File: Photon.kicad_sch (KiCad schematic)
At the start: 39 parts, among them P1 USB_C_Plug_USB2.0, SW1 TS-1088-AR02016, SW2 TS-1088-AR02016, U1 ATtiny13A-S, U2 RT8059GJ5, U3 BCR421UW6-7, U4 BCR421UW6-7, U5 TP4056, U6 FS8205A, U7 DW01A

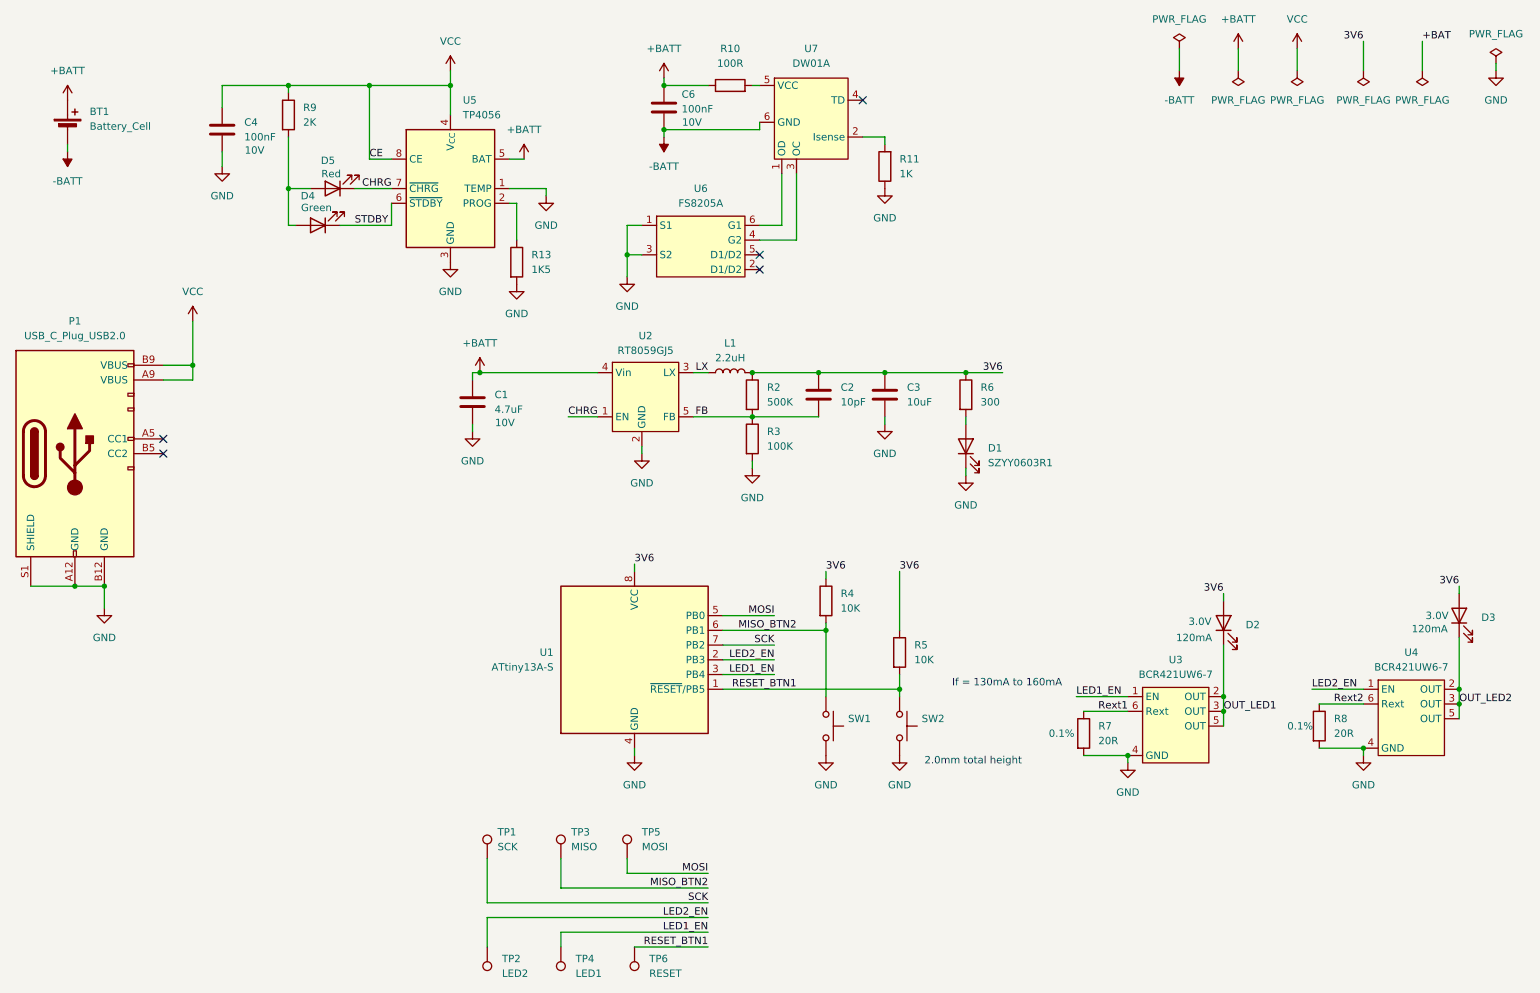
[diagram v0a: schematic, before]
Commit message: made new pcb. and updated schematic
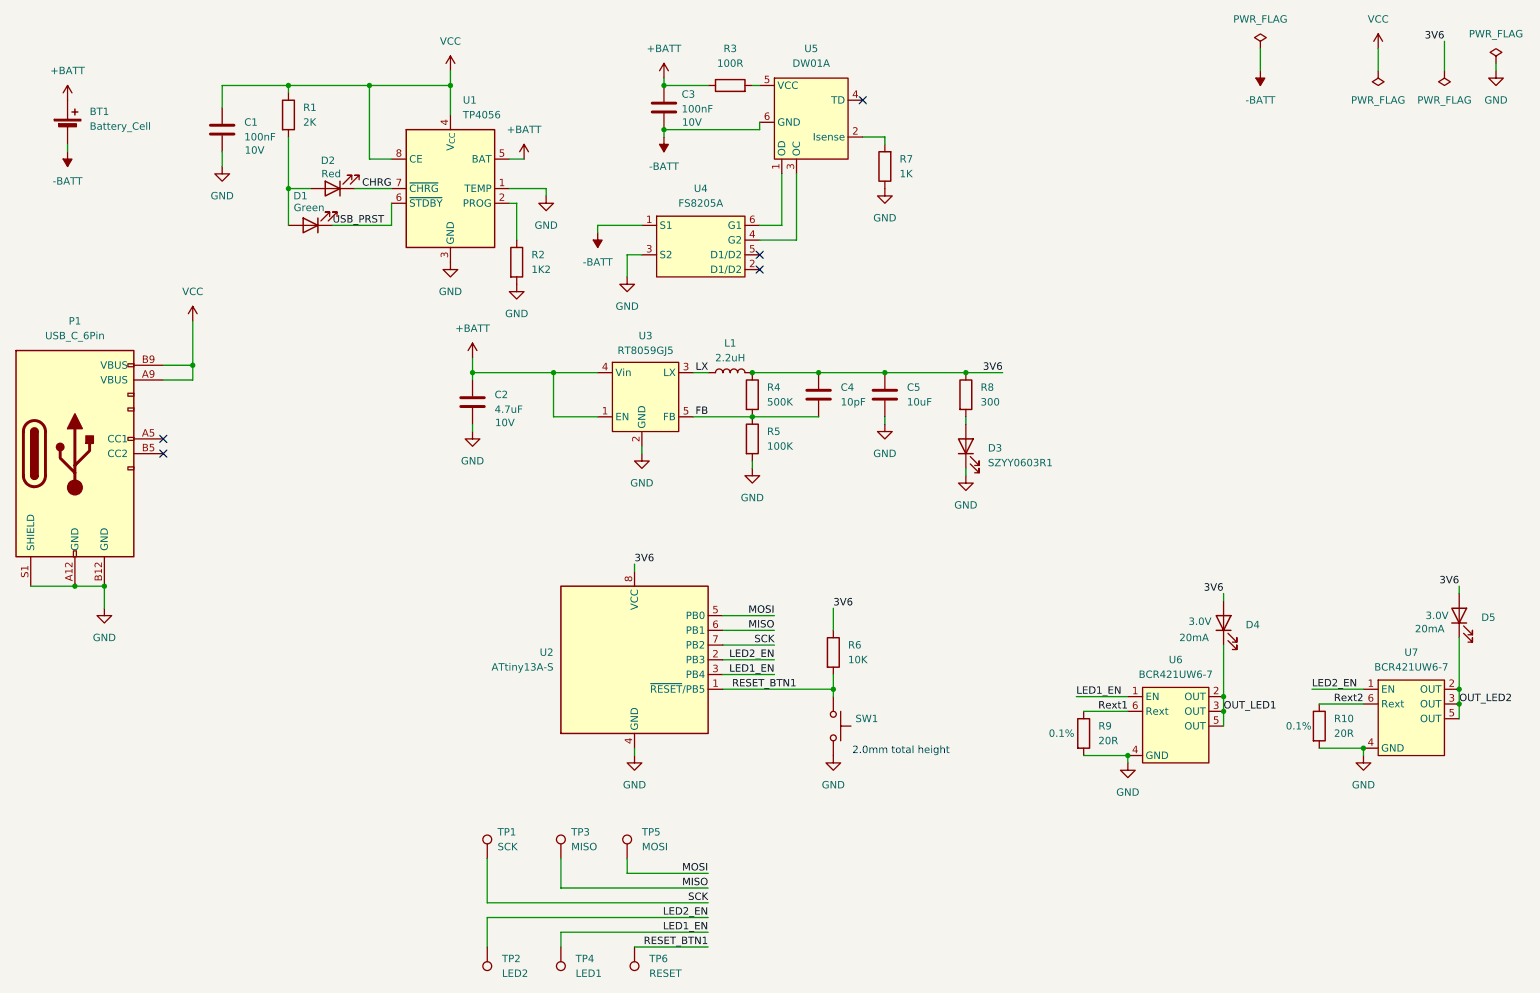
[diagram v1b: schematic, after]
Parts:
- removed R4: 10K, Resistor_SMD:R_0603_1608Metric, symbol Device:R
- removed SW1: TS-1088-AR02016, Photon:5mm Push Button, symbol Switch:SW_Push
- D4: renamed from D2; If 120mA -> 20mA
- D5: renamed from D3; If 120mA -> 20mA
- P1: value USB_C_Plug_USB2.0 -> USB_C_6Pin; footprint Photon:USB_C_Through_Hole -> Connector_USB:USB_C_Receptacle_GCT_USB4125-xx-x-0190_6P_TopMnt_Horizontal
- R2: renamed from R13; value 1K5 -> 1K2
- renumbered C4 to C1, C1 to C2, C6 to C3, C2 to C4, C3 to C5, D4 to D1, D5 to D2, D1 to D3, R9 to R1, R8 to R10, R10 to R3, R2 to R4, R3 to R5, R5 to R6, R11 to R7, R6 to R8, R7 to R9, SW2 to SW1, U5 to U1, U1 to U2, U2 to U3, U6 to U4, U7 to U5, U3 to U6, U4 to U7
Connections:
- net +BATT: now also U3.1 (EN)
- net -BATT: now also U4.1 (S1)
- net CHRG: no longer U3.1 (EN)
- net GND: no longer U4.1 (S1)
- net MISO_BTN2 renamed MISO
- net STDBY renamed USB_PRST
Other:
- note removed: "If = 130mA to 160mA"
- moved on the sheet: D1, R6, SW1

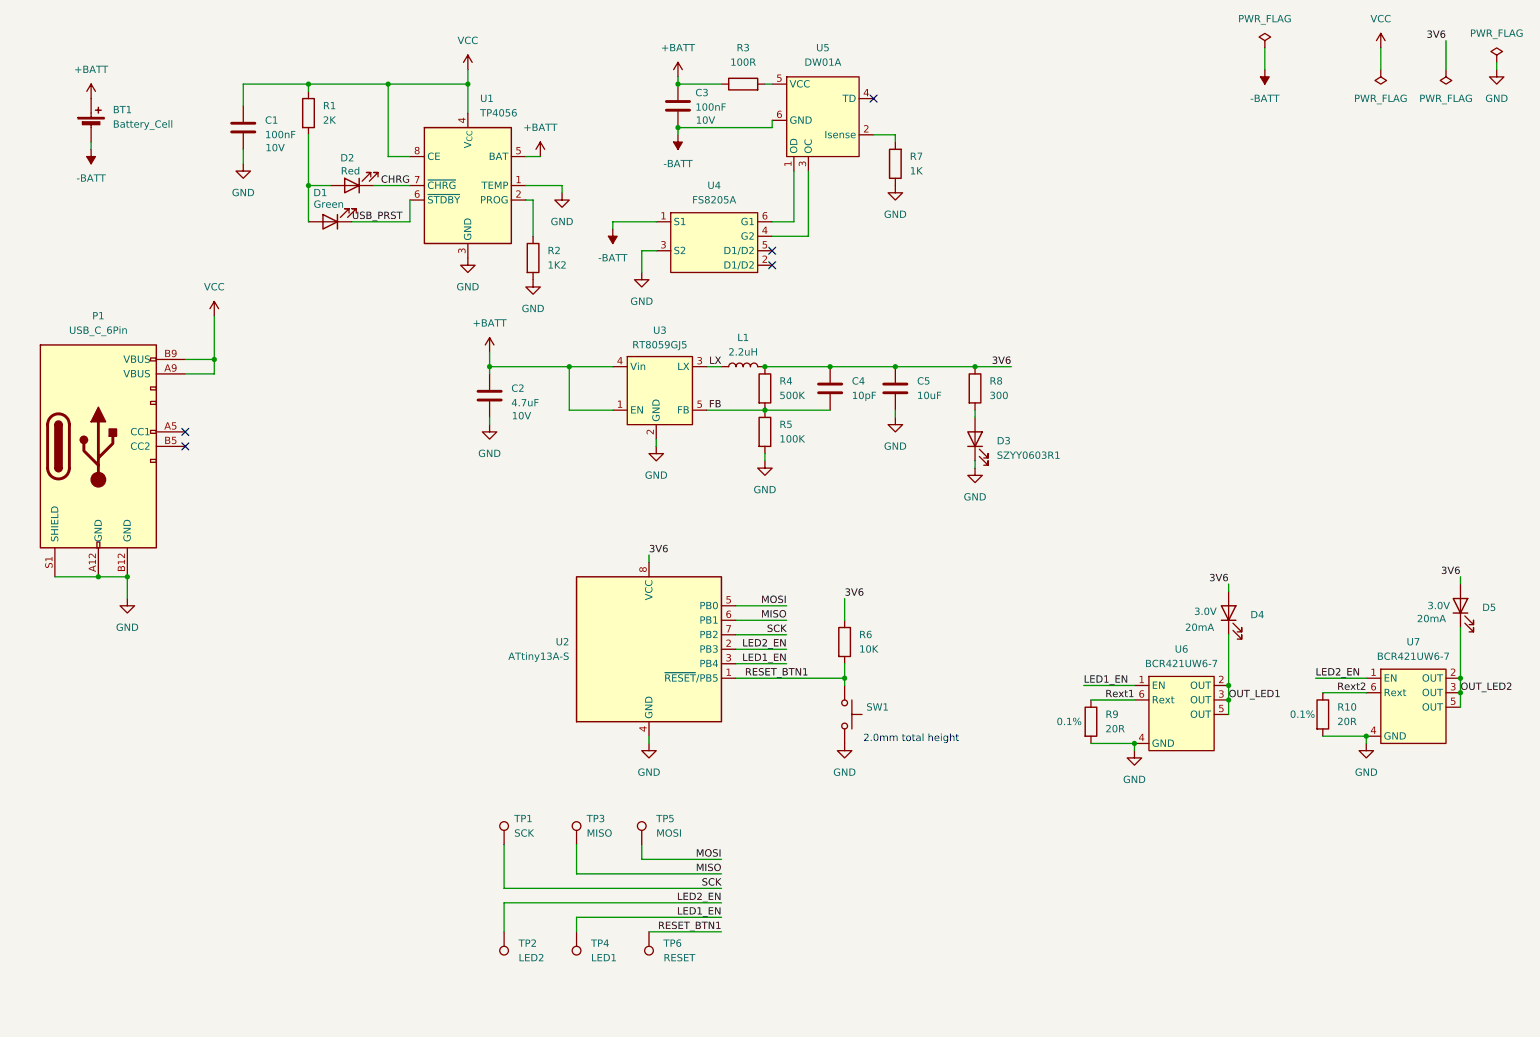
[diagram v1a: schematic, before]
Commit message: Cleaned up schematic and PCB
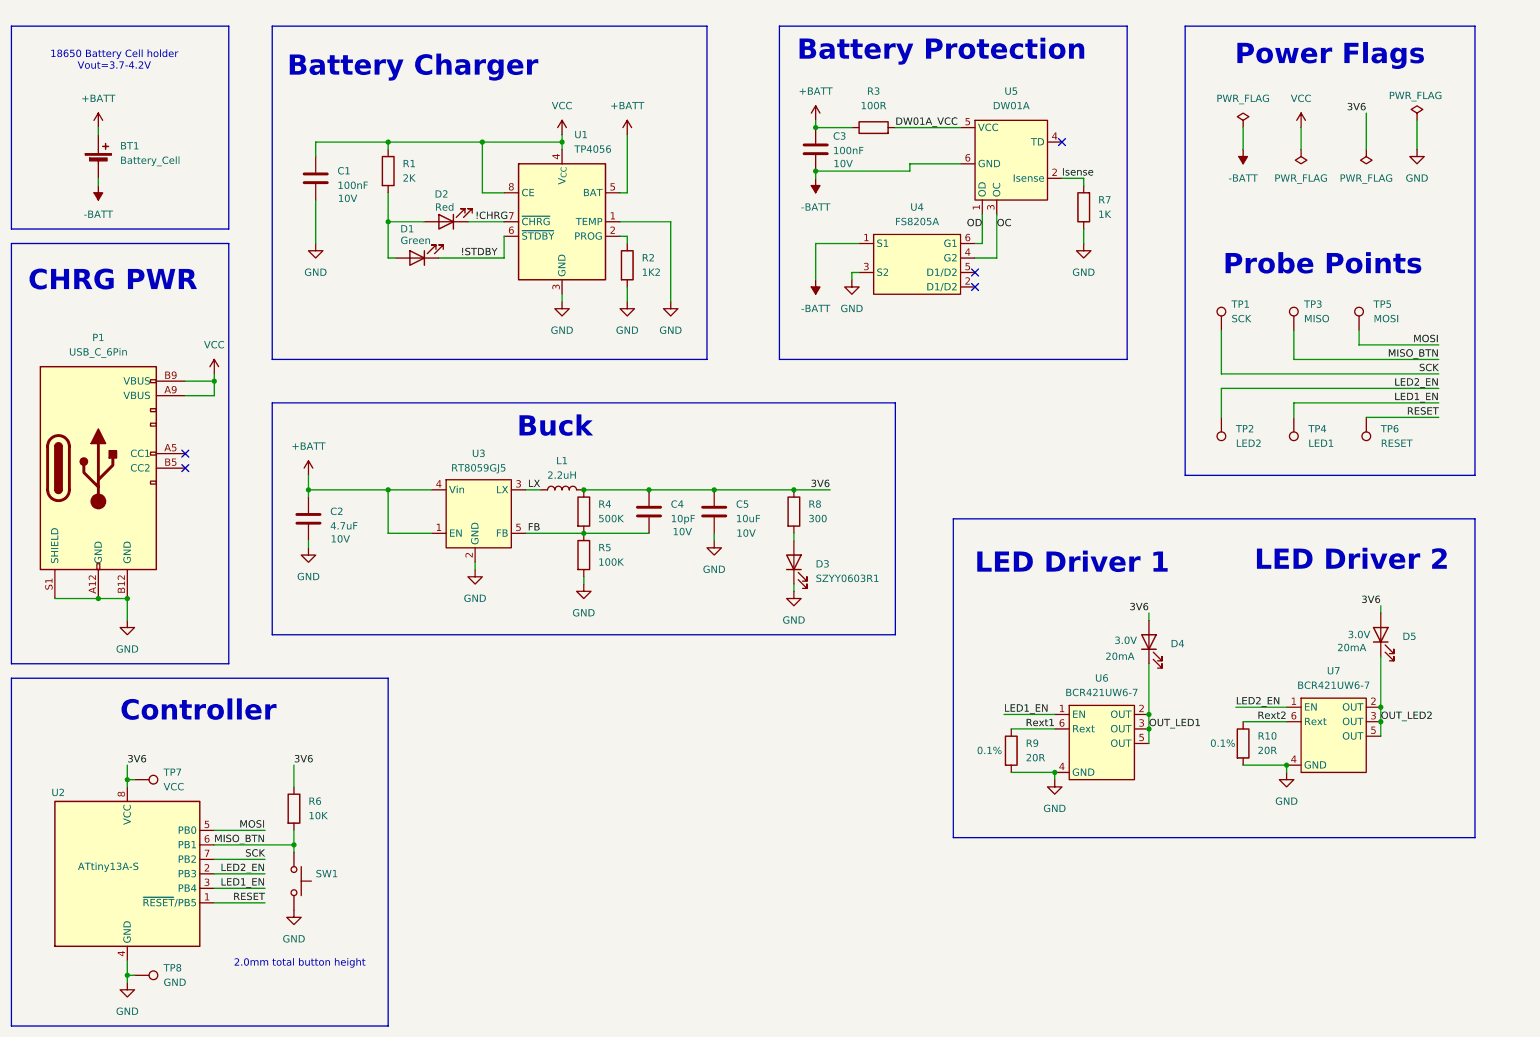
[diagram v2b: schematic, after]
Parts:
- added TP7: VCC, TestPoint:TestPoint_Pad_D1.0mm, symbol Connector:TestPoint
- added TP8: GND, TestPoint:TestPoint_Pad_D1.0mm, symbol Connector:TestPoint
- C4: Voltage (none) -> 10V
- C5: Voltage rating (none) -> 10V
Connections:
- net 3V6: now also TP7.1
- net GND: now also TP8.1
- net OD: now reaches U4.6 (G1), U5.1 (OD)
- net Isense: now reaches R7.2, U5.2 (Isense)
- net OC: now reaches U4.4 (G2), U5.3 (OC)
- net DW01A_VCC: now reaches R3.2, U5.5 (VCC)
- net CHRG renamed !CHRG
- net MISO renamed MISO_BTN
- net MISO_BTN: now also R6.2, SW1.1
- net RESET_BTN1 renamed RESET
- net RESET: no longer R6.2, SW1.1
- net USB_PRST renamed !STDBY
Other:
- note added: "18650 Battery Cell holder Vout=3.7-4.2V"
- note added: "2.0mm total button height"
- note added: "Battery Charger"
- note added: "Battery Protection"
- note added: "Buck"
- note added: "CHRG PWR"
- note added: "Controller"
- note added: "LED Driver 1"
- note added: "LED Driver 2"
- note added: "Power Flags"
- note added: "Probe Points"
- note removed: "2.0mm total height"
- company: (none) -> Bike LED Schematic
- title: (none) -> Photon 
- moved on the sheet: BT1, C1, C2, C3, C4, C5, D1, D2, D3, D4, D5, L1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

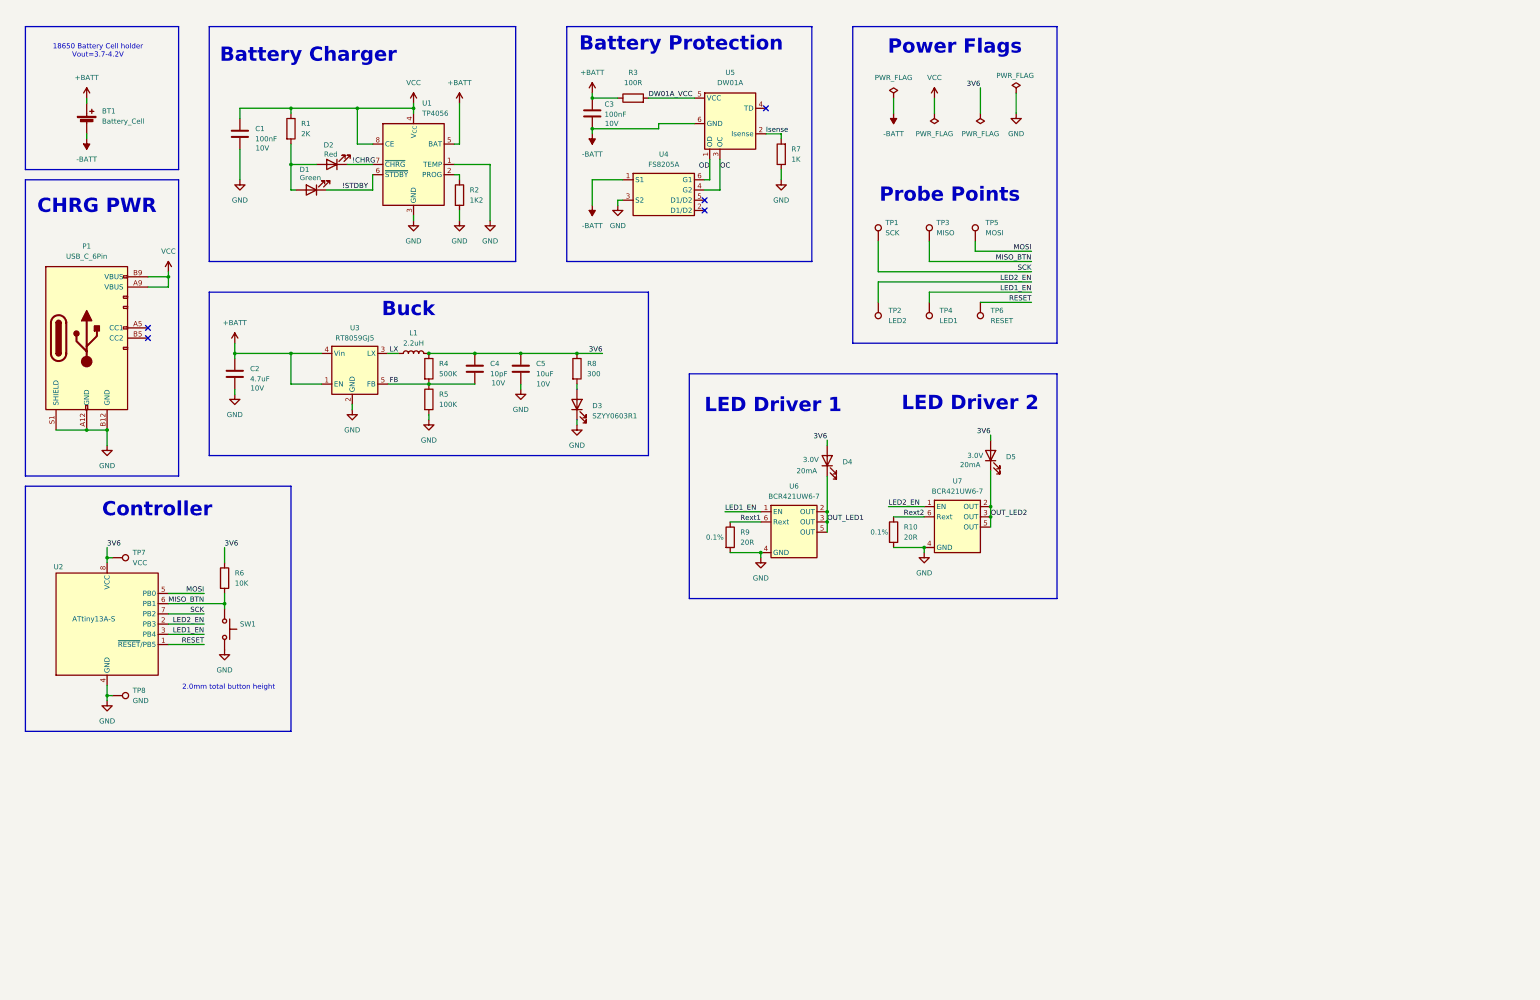
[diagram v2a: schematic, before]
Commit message: New Battery IC
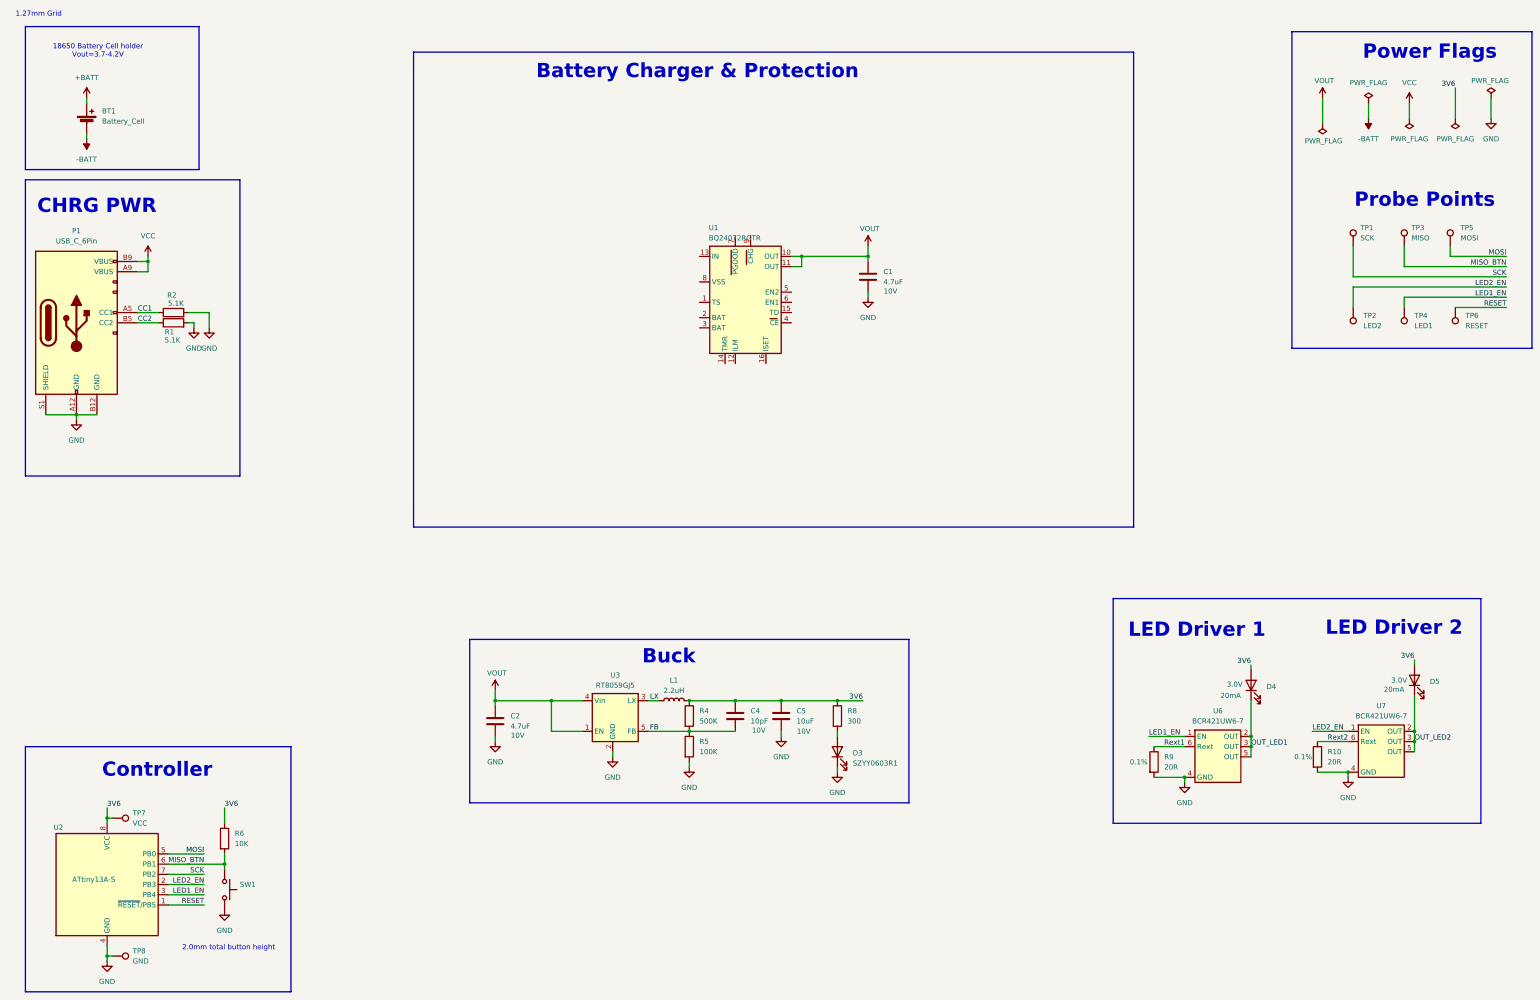
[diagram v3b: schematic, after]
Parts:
- removed C3: 100nF, Capacitor_SMD:C_0603_1608Metric, symbol Device:C
- removed D1, D2: SZYY0603R1, LED_SMD:LED_0603_1608Metric, symbol Device:LED
- removed R3: 100R, Resistor_SMD:R_0603_1608Metric, symbol Device:R
- removed R7: 1K, Resistor_SMD:R_0603_1608Metric, symbol Device:R
- removed U1: TP4056, Package_SO:SOIC-8-1EP_3.9x4.9mm_P1.27mm_EP2.41x3.3mm, symbol Battery_Management:TP4056-42-ESOP8
- removed U4: FS8205A, Package_TO_SOT_SMD:SOT-23-6, symbol Photon:FS8205A
- removed U5: DW01A, Package_TO_SOT_SMD:SOT-23-6, symbol Photon:DW01A
- added U1: BQ24072RGTR, symbol Photon:BQ24074RGTR
- C1: value 100nF -> 4.7uF
- R1: value 2K -> 5.1K
- R2: value 1K2 -> 5.1K
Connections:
- net +BATT: no longer C2.2, U3.1 (EN), U3.4 (Vin)
- net GND: now also R1.2
- net VCC: no longer C1.2, R1.1
- net CC1: now reaches R2.1
- net CC1: now also P1.A5 (CC1)
- net CC2: now reaches P1.B5 (CC2)
- net CC2: now also R1.1
- new net VOUT: C1.2, C2.2, U1.10 (OUT), U1.11 (OUT), U3.1 (EN), U3.4 (Vin)
- no-connect marks 5 -> 0
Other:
- note added: "1.27mm Grid"
- note added: "Battery Charger & Protection"
- note removed: "Battery Charger"
- note removed: "Battery Protection"
- moved on the sheet: C2, C4, C5, D3, D4, D5, L1, P1, R10, R4, R5, R6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
